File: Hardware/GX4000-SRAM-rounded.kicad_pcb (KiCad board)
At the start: 4 copper layers, 10.2 x 52.1 mm, 11 parts, among them IC10 TMS4464, IC11 TMS4464, U1 IS61C1024AL-12HLI, U2 74HCT573, U3 74LVC1G32, U4 74LVC1G08

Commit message: v2.1
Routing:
- net VCC: track 54.7 -> 56.5 mm
- net /MA4: track 37.5 -> 36.2 mm
- net /MA3: track 38.6 -> 37.4 mm
- net /D0: track 23.9 -> 22.9 mm
- net /MA1: track 32.3 -> 31.5 mm
- net /A4: track 9.41 -> 8.57 mm
- net /MA6: track 30.5 -> 29.7 mm
- net /D1: track 26.2 -> 25.6 mm
- net /A5: track 8.26 -> 7.65 mm
- net Net-(U1-Pad30): track 25.5 -> 25.0 mm
- net /A0: track 8.87 -> 8.33 mm
- net /MA2: track 37.4 -> 36.9 mm
- net /MA0: track 29.0 -> 28.5 mm

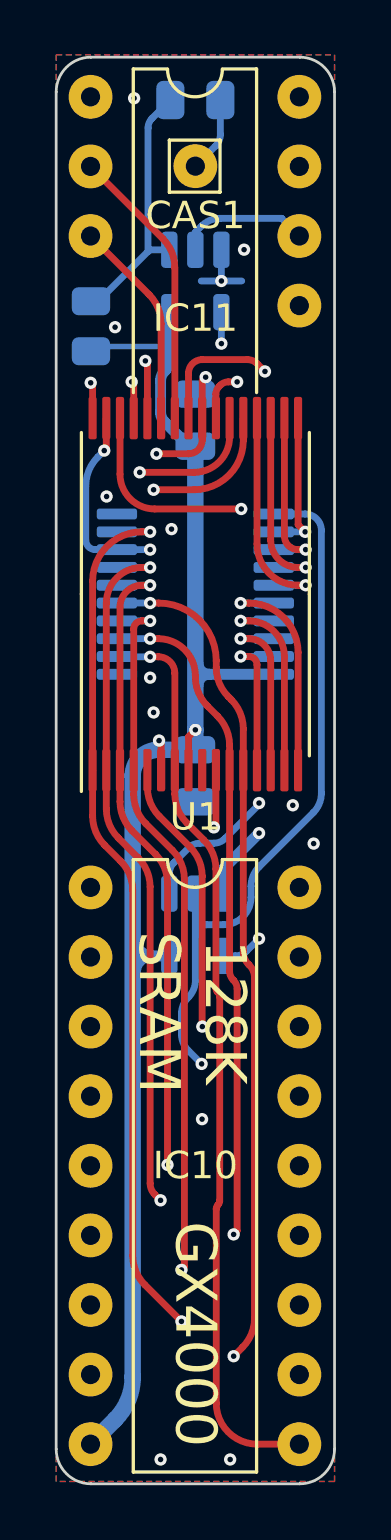
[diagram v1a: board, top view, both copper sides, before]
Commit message: Update Kicad version to 8
- Update Kicad version format
- Update Footprint
- Add JLCPCB component reference
- Add BOM in description
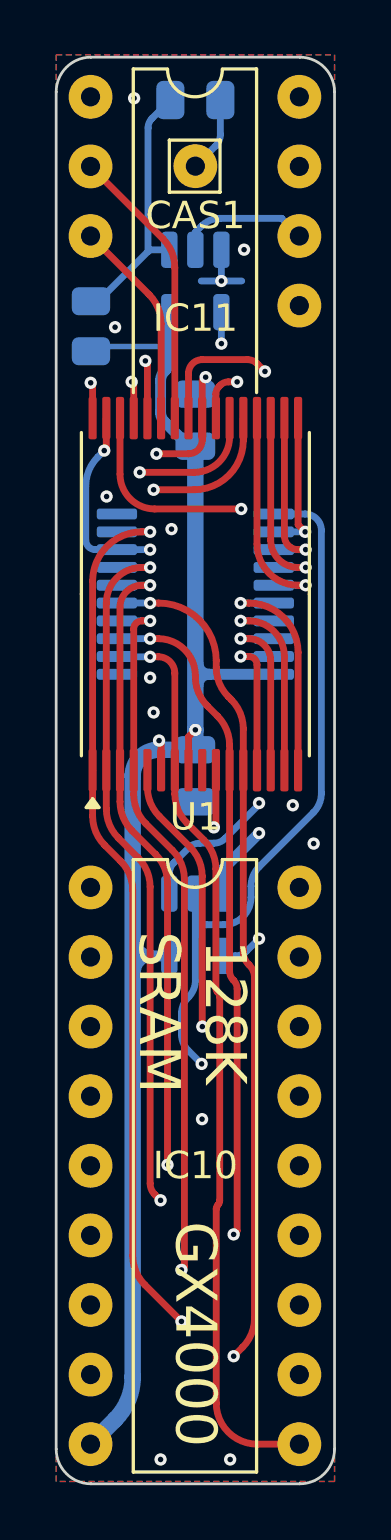
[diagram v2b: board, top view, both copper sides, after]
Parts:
- U2: value 74HCT573 -> SN74HCT573PWR
- turned R1 to 90 degrees
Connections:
- R1 pad 1: /~{CAS1} -> VCC
- R1 pad 2: VCC -> /~{CAS1}
